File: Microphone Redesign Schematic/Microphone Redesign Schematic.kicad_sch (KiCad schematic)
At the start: 17 parts, among them J1 Custom_3p_2.0MM, U1 ${SIM.PARAMS}

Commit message: updated shcematics after meeting 1/21/26
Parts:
- removed J1: Custom_3p_2.0MM, symbol Connector_Generic:Conn_01x03
- added I1: IPWL, symbol Simulation_SPICE:IPWL
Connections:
- net 0: now also I1.2
- net at R32.2: now also I1.1
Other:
- moved on the sheet: C14, C17, C18, C19, C26, C27, R1, R18, R19, R27, R32, R36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

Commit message: 1/26 edit SPICE modeling
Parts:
- removed TP3: TP TH Round 45 mil sqr, 25mil hole, symbol Connector:TestPoint
- R36: value 0 -> 1.000000e-12
- V1: renamed from I1; value IPWL -> VPWL
- V3: value 3V -> 3.3V
- renumbered V3 to V4
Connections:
- net LPF: now reaches C18.1, C19.1, R1.2, R32.1
- net Notch: now reaches C17.1, C18.2, R1.1, R27.1, U1.1 (+)
- net PWL: now reaches R32.2, V1.1
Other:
- moved on the sheet: C19
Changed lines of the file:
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@@
-	)
-	(junction
-		(at 102.87 114.3)
-		(diameter 0)
-		(color 0 0 0 0)
 	)
 	(junction
@@
 	)
 	(junction
-		(at 224.79 110.49)
+		(at 95.25 114.3)
 		(diameter 0)
 		(color 0 0 0 0)
@@
 	(wire
 		(pts
-			(xy 102.87 114.3) (xy 113.03 114.3)
-		)
-		(stroke
-			(width 0)
-			(type default)
-		)
-	)
-	(wire
-		(pts
 			(xy 41.91 55.88) (xy 30.48 55.88)
 		)
@@
 	(wire
 		(pts
-			(xy 215.9 110.49) (xy 224.79 110.49)
+			(xy 215.9 110.49) (xy 248.92 110.49)
 		)
 		(stroke
@@
 	(wire
 		(pts
+			(xy 95.25 114.3) (xy 113.03 114.3)
+		)
+		(stroke
+			(width 0)
+			(type default)
+		)
+	)
+	(wire
+		(pts
 			(xy 64.77 96.52) (xy 73.66 96.52)
 		)
@@
 	(wire
 		(pts
-			(xy 91.44 114.3) (xy 102.87 114.3)
+			(xy 91.44 114.3) (xy 95.25 114.3)
 		)
 		(stroke
@@
 	(wire
 		(pts
-			(xy 102.87 114.3) (xy 102.87 120.65)
+			(xy 95.25 114.3) (xy 95.25 120.65)
 		)
 		(stroke
@@
 	(wire
 		(pts
-			(xy 102.87 128.27) (xy 102.87 133.35)
+			(xy 95.25 128.27) (xy 95.25 133.35)
 		)
 		(stroke
@@
 		)
 	)
-	(wire
-		(pts
-			(xy 224.79 110.49) (xy 248.92 110.49)
-		)
-		(stroke
-			(width 0)
-			(type default)
+	(label "Notch"
+		(at 158.75 107.95 0)
+		(effects
+			(font
+				(size 1.27 1.27)
+			)
+			(justify left bottom)
+		)
+	)
+	(label "LPF"
+		(at 102.87 114.3 0)
+		(effects
+			(font
+				(size 1.27 1.27)
+			)
+			(justify left bottom)
 		)
 	)
 	(label "ENV_OUT"
 		(at 248.92 110.49 0)
+		(effects
+			(font
+				(size 1.27 1.27)
+			)
+			(justify left bottom)
+		)
+	)
+	(label "PWL"
+		(at 41.91 114.3 0)
 		(effects
 			(font
@@
 	(symbol
 		(lib_id "Device:C")
-		(at 102.87 124.46 0)
+		(at 95.25 124.46 0)
 		(unit 1)
 		(exclude_from_sim no)
@@
 		(fields_autoplaced yes)
 		(property "Reference" "C19"
-			(at 106.68 123.1899 0)
+			(at 99.06 123.1899 0)
 			(effects
 				(font
@@
 		)
 		(property "Value" "0.1u"
-			(at 106.68 125.7299 0)
+			(at 99.06 125.7299 0)
 			(effects
 				(font
@@
 		)
 		(property "Footprint" ""
-			(at 103.8352 128.27 0)
+			(at 96.2152 128.27 0)
 			(effects
 				(font
@@
 		)
 		(property "Datasheet" "~"
-			(at 102.87 124.46 0)
+			(at 95.25 124.46 0)
 			(effects
 				(font
@@
 		)
 		(property "Description" "Unpolarized capacitor"
-			(at 102.87 124.46 0)
+			(at 95.25 124.46 0)
 			(effects
 				(font
@@
 	(symbol
 		(lib_id "Simulation_SPICE:0")
-		(at 102.87 133.35 0)
+		(at 95.25 133.35 0)
 		(unit 1)
 		(exclude_from_sim no)
@@
 		(fields_autoplaced yes)
 		(property "Reference" "#GND03"
-			(at 102.87 138.43 0)
+			(at 95.25 138.43 0)
 			(effects
 				(font
@@
 		)
 		(property "Value" "0"
-			(at 102.87 130.81 0)
+			(at 95.25 130.81 0)
 			(effects
 				(font
@@
 		)
 		(property "Footprint" ""
-			(at 102.87 133.35 0)
+			(at 95.25 133.35 0)
 			(effects
 				(font
@@
 		)
 		(property "Datasheet" "https://ngspice.sourceforge.io/docs/ngspice-html-manual/manual.xhtml#subsec_Circuit_elements__device"
-			(at 102.87 143.51 0)
+			(at 95.25 143.51 0)
 			(effects
 				(font
@@
 		)
 		(property "Description" "0V reference potential for simulation"
-			(at 102.87 140.97 0)
+			(at 95.25 140.97 0)
 			(effects
 				(font
@@
 			)
 		)
-		(property "Value" "3V"
+		(property "Value" "3.3V"
 			(at 177.8 83.6901 0)
 			(effects
@@
 				(path "/596682a8-368c-4487-88dd-7dc1689f5b13"
 					(reference "V3")
-					(unit 1)
-				)
-			)
-		)
-	)
-	(symbol
-		(lib_id "Connector:TestPoint")
-		(at 224.79 110.49 0)
-		(unit 1)
-		(exclude_from_sim no)
-		(in_bom yes)
-		(on_board yes)
-		(dnp no)
-		(property "Reference" "TP3"
-			(at 224.79 102.108 0)
-			(effects
-				(font
-					(size 1.27 1.27)
-				)
-				(justify left)
-			)
-		)
-		(property "Value" "TP TH Round 45 mil sqr, 25mil hole"
-			(at 224.79 104.1401 0)
-			(effects
-				(font
-					(size 1.27 1.27)
-				)
-				(justify left)
-			)
-		)
-		(property "Footprint" ""
-			(at 229.87 110.49 0)
-			(effects
-				(font
-					(size 1.27 1.27)
-				)
-				(hide yes)
-			)
-		)
-		(property "Datasheet" "~"
-			(at 229.87 110.49 0)
-			(effects
-				(font
-					(size 1.27 1.27)
-				)
-				(hide yes)
-			)
-		)
-		(property "Description" "test point"
-			(at 224.79 110.49 0)
-			(effects
-				(font
-					(size 1.27 1.27)
-				)
-				(hide yes)
-			)
-		)
-		(pin "1"
-		)
-		(instances
-			(project ""
-				(path "/596682a8-368c-4487-88dd-7dc1689f5b13"
-					(reference "TP3")
 					(unit 1)
 				)
@@
 		(dnp no)
 		(fields_autoplaced yes)
-		(property "Reference" "I1"
-			(at 36.83 118.1099 0)
-			(effects
-				(font
-					(size 1.27 1.27)
-				)
-				(justify left)
-			)
-		)
-		(property "Value" "IPWL"
-			(at 36.83 120.6499 0)
+		(property "Reference" "V1"
+			(at 36.83 119.3799 0)
+			(effects
+				(font
+					(size 1.27 1.27)
+				)
+				(justify left)
+			)
+		)
+		(property "Value" "VPWL"
+			(at 36.83 121.9199 0)
 			(effects
 				(font
@@
 		)
 		(property "Sim.Type" "PWL"
+			(at 33.02 120.65 0)
+			(effects
+				(font
+					(size 1.27 1.27)
+				)
+				(hide yes)
+			)
+		)
+		(property "Sim.Params" "pwl=\"0 0.40 0.001 0.46 0.002 0.43 0.003 0.46 0.004 0.46 0.005 0.50 0.006 0.50 0.007 0.53 0.008 0.57 0.009 0.60 0.010 0.70 0.011 0.77 0.012 0.87 0.013 0.97 0.014 0.97 0.015 0.90 0.016 0.70 0.017 0.67 0.018 0.53 0.019 0.46 0.020 0.50 0.021 0.50 0.022 0.50\""
 			(at 33.02 120.65 0)
 			(effects
@@
 			(project ""
 				(path "/596682a8-368c-4487-88dd-7dc1689f5b13"
-					(reference "I1")
+					(reference "V1")
 					(unit 1)
 				)
@@
 		(dnp no)
 		(fields_autoplaced yes)
-		(property "Reference" "V3"
+		(property "Reference" "V4"
 			(at 34.29 69.7201 0)
 			(effects
@@
 			(project ""
 				(path "/596682a8-368c-4487-88dd-7dc1689f5b13"
-					(reference "V3")
+					(reference "V4")
 					(unit 1)
 				)
@@
 			)
 		)
-		(property "Value" "0"
+		(property "Value" "1.000000e-12"
 			(at 60.96 92.71 90)
 			(effects

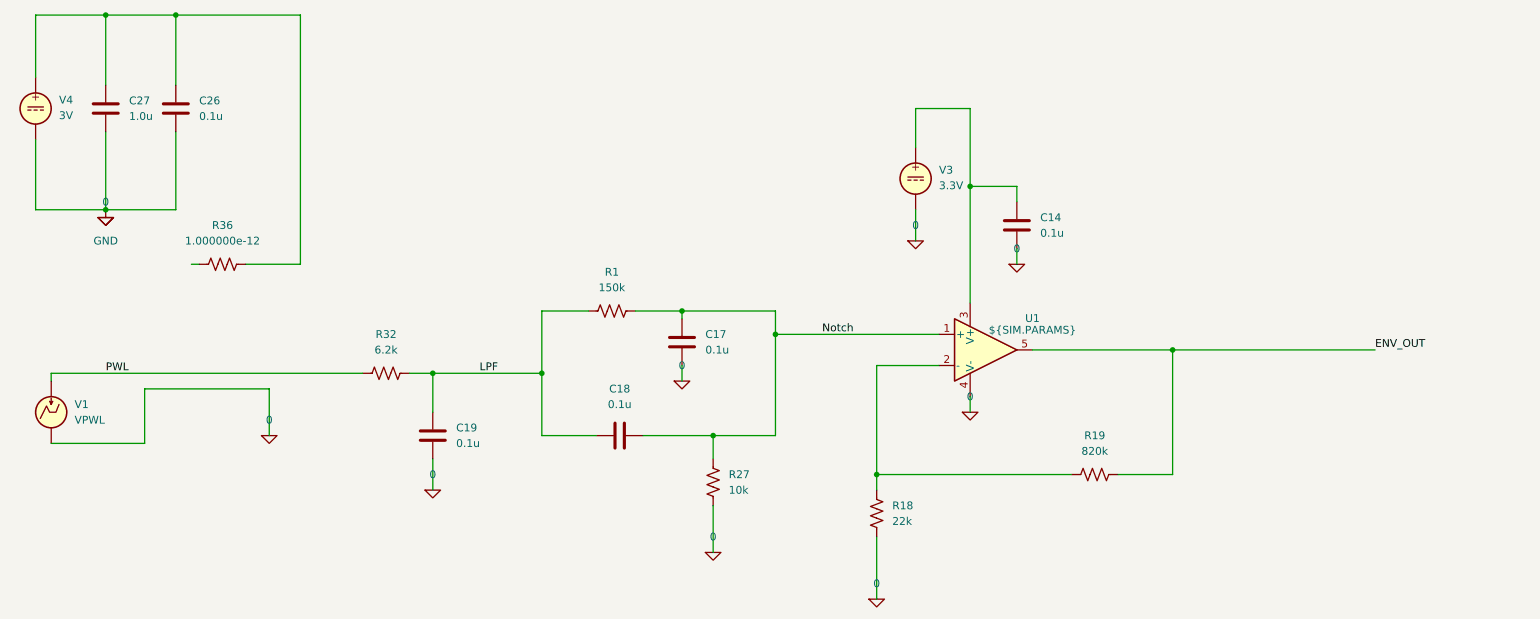
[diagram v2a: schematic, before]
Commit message: notch filter redesign 1/28
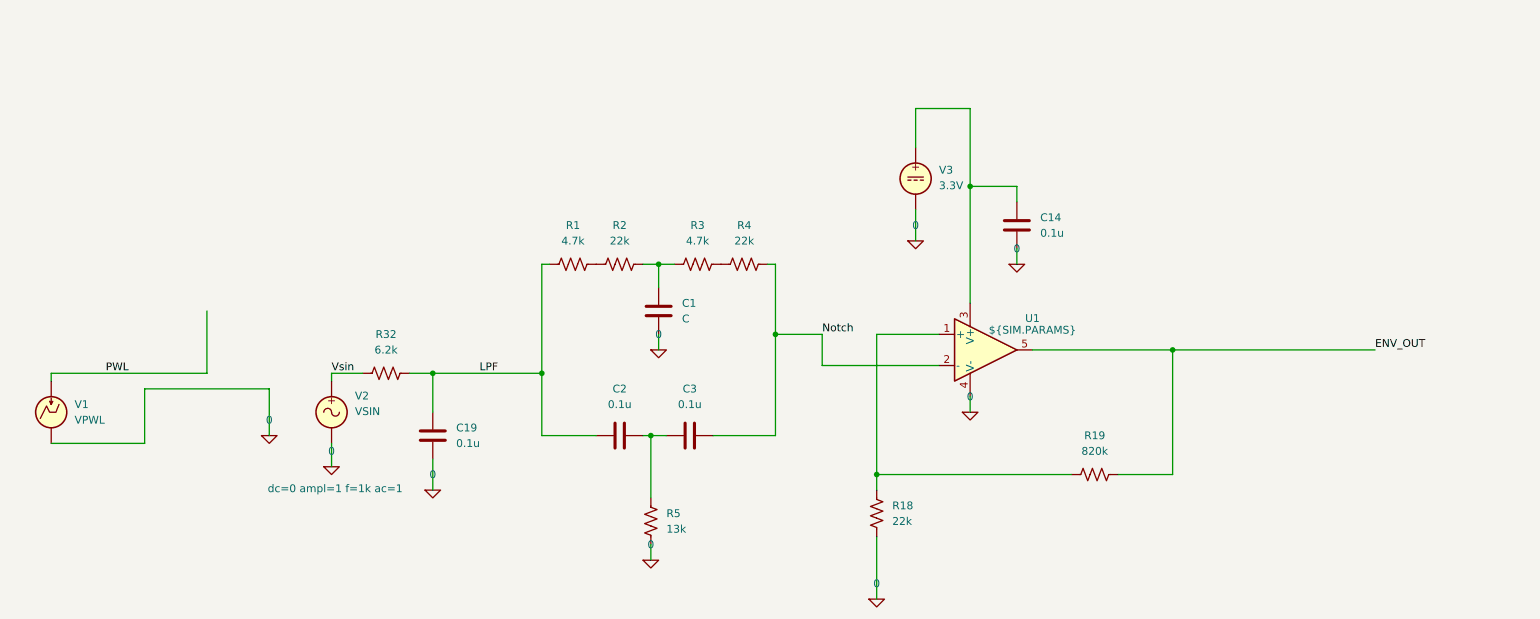
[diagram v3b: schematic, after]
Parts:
- removed C17, C18, C26: 0.1u, symbol Device:C
- removed C27: 1.0u, symbol Device:C
- removed R27: 10k, symbol Device:R_US
- removed R36: 1.000000e-12, symbol Device:R_US
- removed V4: 3V, symbol Simulation_SPICE:VDC
- added C1: C, symbol Device:C
- added C2, C3: 0.1u, symbol Device:C
- added R2, R4: 22k, symbol Device:R_US
- added R3: 4.7k, symbol Device:R_US
- added R5: 13k, symbol Device:R_US
- added V2: VSIN, symbol Simulation_SPICE:VSIN
- R1: value 150k -> 4.7k
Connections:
- net 0: now also C1.2, R5.2, V2.2
- net LPF: now also R1.1, C2.1; no longer R1.2
- net Notch: now also U1.2 (-), C3.2, R4.2; no longer R1.1, U1.1 (+)
- net PWL: no longer R32.2
- net at R18.1, R19.2: now also U1.1 (+); no longer U1.2 (-)
- new net: C2.2, C3.1, R5.1
- new net: R1.2, R2.1
- new net: C1.1, R2.2, R3.1
- new net: R3.2, R4.1
- new net Vsin: R32.2, V2.1
